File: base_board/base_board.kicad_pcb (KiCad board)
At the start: 6 copper layers, 50 x 50 mm, 54 parts, among them J1 Conn_ARM_JTAG_SWD_20, J2 Conn_01x20_Pin, J3 Conn_01x20_Socket, SW1 SW_Push, U1 STM32F446ZEJx, U2 IS42S16400J-xT, U3 BMI270, U4 USB_C_Receptacle_USB2.0, U5 10p, U6 10p, U7 LD3985M33R_SOT23, Y1 Crystal_GND24

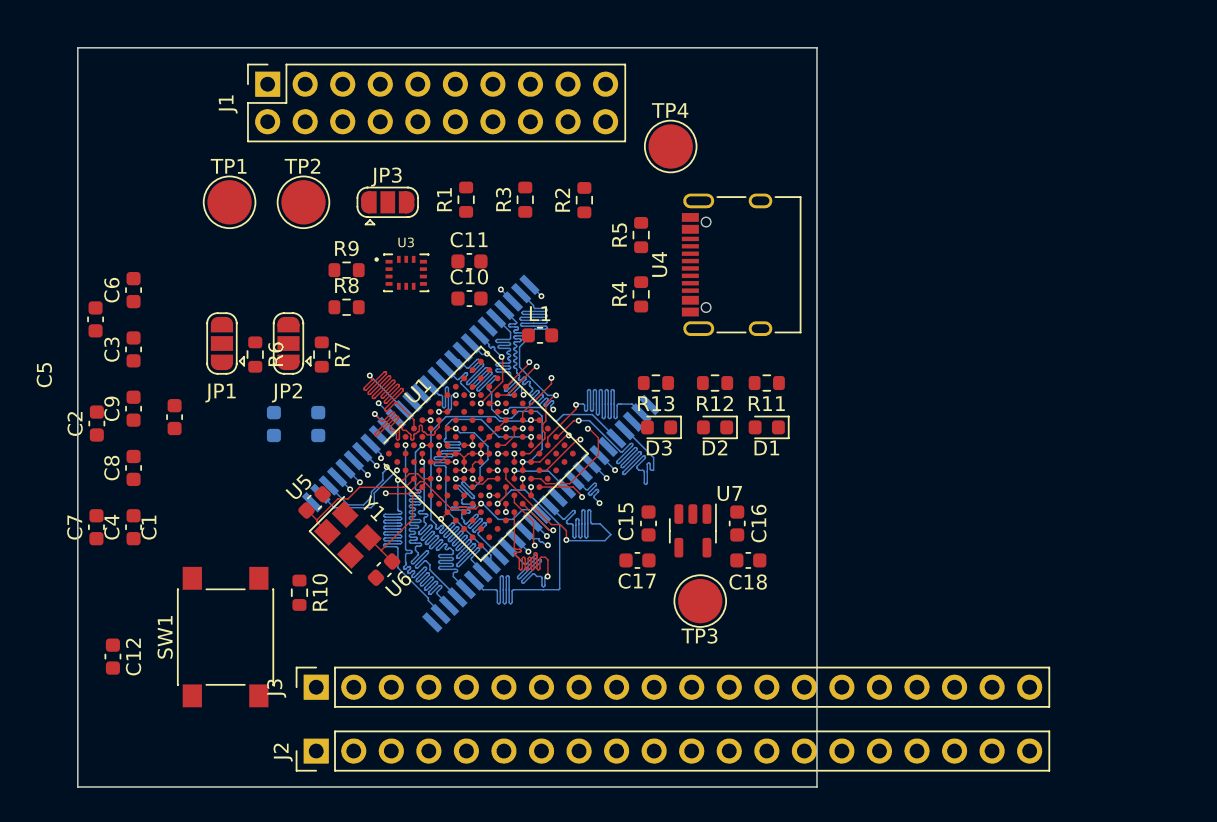
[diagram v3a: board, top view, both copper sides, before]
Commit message: [pcb] added route for BMI270
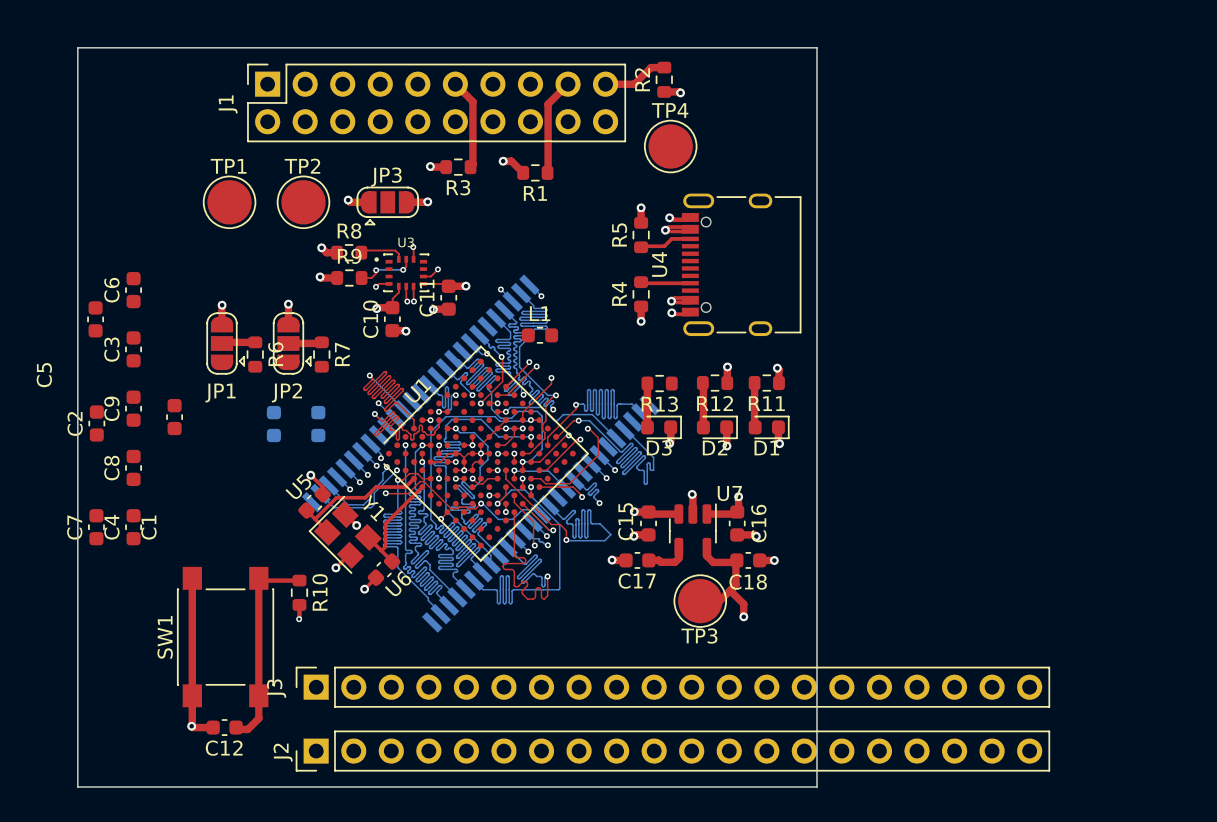
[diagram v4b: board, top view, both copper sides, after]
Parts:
- moved R2 9.78 mm to (142.7, 70.2)
- moved C12 8.95 mm to (112.9, 114.0), turned to 180 degrees
- moved C10 5.39 mm to (124.3, 86.4), turned to 90 degrees
- moved R3 5.03 mm to (128.7, 76.1), turned to 180 degrees
- moved R1 5.02 mm to (133.9, 76.5), turned to 180 degrees
- moved R8 3.69 mm to (121.4, 81.9)
- moved C11 2.83 mm to (128.1, 84.9), turned to 90 degrees
- moved R9 0.56 mm to (121.4, 83.6)
- moved R13 0.25 mm to (142.4, 90.7)
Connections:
- C10 pad 2: +3.3V -> +3V3
- C11 pad 2: +3.3V -> +3V3
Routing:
- net +3V3: track 0.00 -> 124.2 mm, vias 0 -> 11
- net +5V: track 0.00 -> 48.3 mm, vias 0 -> 5
- net GND: track 7.01 -> 47.1 mm, vias 6 -> 31
- net /RESET: track 0.00 -> 14.2 mm
- net Net-(J1-DBGRQ/NC): track 0.00 -> 6.57 mm
- net Net-(J1-RTCK): track 0.00 -> 6.17 mm
- net Net-(J1-DBGACK/NC): track 0.00 -> 4.44 mm
- net /BMI270_SCL: track 0.00 -> 3.96 mm, vias 0 -> 2
- net Net-(U4-CC2): track 0.00 -> 3.56 mm
- net Net-(U4-CC1): track 0.00 -> 3.36 mm
- net /BMI270_SDA: track 0.00 -> 3.06 mm
- net Net-(D2-A): track 0.00 -> 3.02 mm
- net Net-(D1-A): track 0.00 -> 3.02 mm
- net Net-(D3-A): track 0.00 -> 2.97 mm
- net Net-(U7-BYP): track 0.00 -> 2.94 mm
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
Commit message: Implemented SDRAM routing (#1)
* [pcb] completed sdram routing

* [pcb] added heartbeat led traces

* [pcb] completed routing except VDDUSB

* [pcb] changed routing for 5V power bus

* [pcb] fixed drc violation

* [pcb] added caps for VDDUSB

* [pcb] draft length matching

* [pcb] fixed length matching for sdram memory

* [view][pcb] toggled all layers for pcb

* [pcb] fixed power planes. Fixed traces shape

* [pcb] added review corrections

* [pcb] added M3 holes

* [pcb] added M3 holes

* [pcb] added onboard uart

* [pcb] added gnd+3v3 for uart socket

* [pcb][schematic] fixed VREF connection. Corrected the shape of the length matcher

* [project] updated fp-info-cache

* [pcb] fixed length matching pattern

* [pcb] placed sdram chip at 45 degree angle

* [project] updated fp-info cache
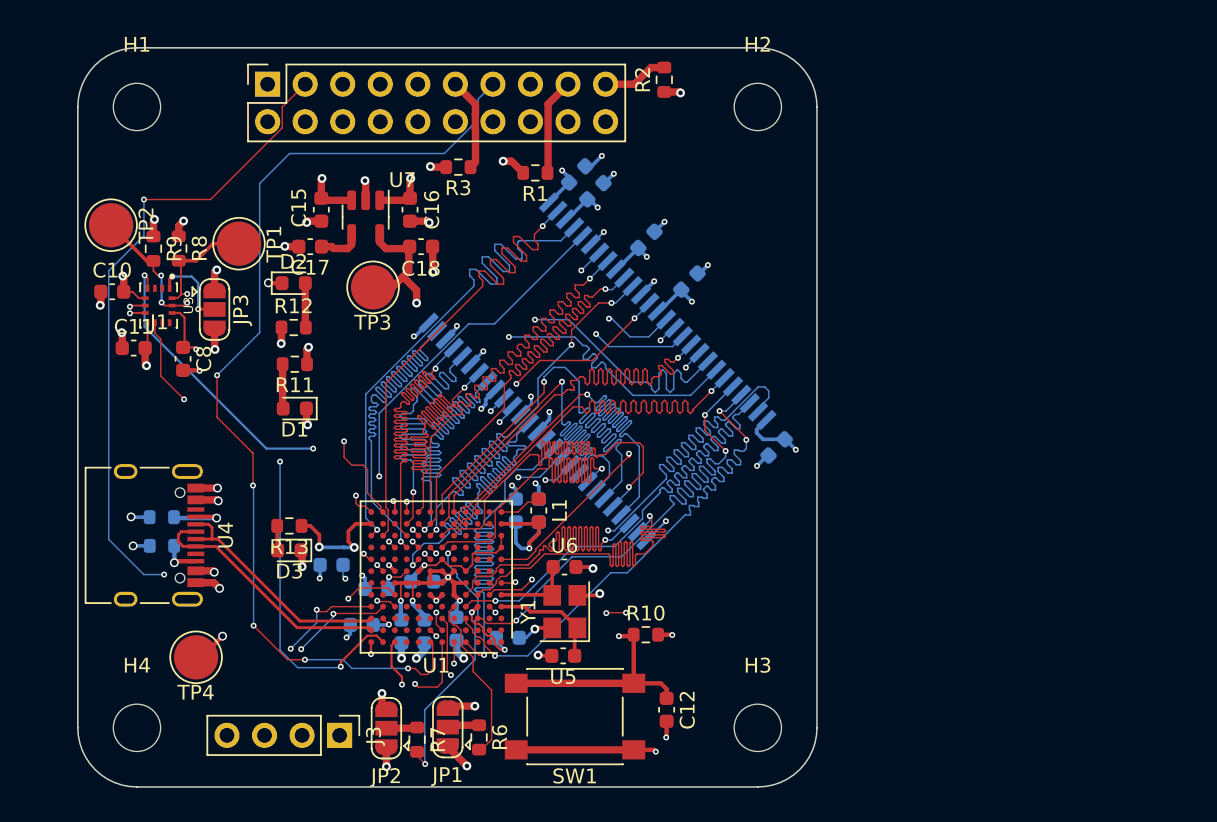
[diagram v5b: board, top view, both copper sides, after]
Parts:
- removed J2: Conn_01x20_Pin, Connector_PinHeader_2.54mm:PinHeader_1x20_P2.54mm_Vertical
- added C19: 100nF, Capacitor_SMD:C_0603_1608Metric, B.Cu at (144.4, 83.8)
- added C20: 100nF, Capacitor_SMD:C_0603_1608Metric, B.Cu at (132.1, 107.9)
- added C21: 1uF, Capacitor_SMD:C_0603_1608Metric, B.Cu at (132.6, 99.3)
- added C22: 100nF, Capacitor_SMD:C_0603_1608Metric, B.Cu at (122.2, 107.0)
- added C23: 100nF, Capacitor_SMD:C_0603_1608Metric, B.Cu at (134.2, 99.3)
- added H1: MountingHole, MountingHole:MountingHole_3.2mm_M3, F.Cu at (107.0, 72.0)
- added H2: MountingHole, MountingHole:MountingHole_3.2mm_M3, F.Cu at (149.0, 72.0)
- added H3: MountingHole, MountingHole:MountingHole_3.2mm_M3, F.Cu at (149.0, 114.0)
- added H4: MountingHole, MountingHole:MountingHole_3.2mm_M3, F.Cu at (107.0, 114.0)
- C1, C2, C3, C4, C5, C6, C7, C9, R4, R5: moved to B.Cu
- J3: value Conn_01x20_Socket -> Conn_01x04; footprint Connector_PinSocket_2.54mm:PinSocket_1x20_P2.54mm_Vertical -> Connector_PinHeader_2.54mm:PinHeader_1x04_P2.54mm_Vertical
- moved TP4 47.2 mm to (111.0, 109.2), turned to 180 degrees
- moved C7 46.3 mm to (150.3, 95.0), turned to -135 degrees
- moved U4 44.7 mm to (107.3, 101.0), turned to -90 degrees
- moved R5 38.6 mm to (108.7, 101.7), turned to 180 degrees
- moved C9 36.5 mm to (141.5, 81.0), turned to 45 degrees
- moved R4 35.8 mm to (108.7, 99.8), turned to 0 degrees
- moved C5 34.0 mm to (136.8, 76.6), turned to 45 degrees
- moved D1 32.0 mm to (117.7, 92.4)
- moved R11 32.0 mm to (117.7, 89.4)
- moved C6 31.9 mm to (138.0, 77.7), turned to 45 degrees
- moved C15 30.7 mm to (119.5, 79.0)
- moved C16 30.7 mm to (125.5, 79.0)
- moved C17 30.7 mm to (118.7, 81.5)
- moved C18 30.7 mm to (126.2, 81.5)
- moved TP3 30.7 mm to (123.0, 84.2)
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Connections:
- C1 pad 1: +3.3V -> +3V3
- C2 pad 1: +3.3V -> +3V3
- C3 pad 1: +3.3V -> +3V3
- C4 pad 1: +3.3V -> +3V3
- C5 pad 1: +3.3V -> +3V3
- C6 pad 1: +3.3V -> +3V3
- C7 pad 1: +3.3V -> +3V3
- C8 pad 1: +3.3V -> +3V3
- C9 pad 1: +3.3V -> +3V3
- J1 pad 1: +3.3V -> +3V3
- J1 pad 2: +3.3V -> +3V3
- J3 pad 1: /PC1 -> GND
- J3 pad 2: /PC2 -> /USART1_RX
- J3 pad 3: /PC3 -> /USART1_TX
- J3 pad 4: /PC4 -> +3V3
- L1 pad 2: +3.3V -> +3V3
- U1 pad C11: Net-(U1-VDDA) -> +3V3
- U1 pad D3: +3.3V -> +3V3
- U1 pad E5: +3.3V -> +3V3
- U1 pad F10: +3.3V -> +3V3
- U1 pad F4: +3.3V -> +3V3
- U1 pad F5: +3.3V -> +3V3
- U1 pad F6: +3.3V -> +3V3
- U1 pad F7: +3.3V -> +3V3
- U1 pad F8: +3.3V -> +3V3
- U1 pad F9: +3.3V -> +3V3
- U1 pad G5: +3.3V -> +3V3
- U1 pad G6: +3.3V -> +3V3
- U1 pad G7: +3.3V -> +3V3
- U1 pad K1: unconnected-(U1-VREF--PadK1) -> GND
- U1 pad L1: unconnected-(U1-VREF+-PadL1) -> +3V3
- U2 pad 1: Net-(U2-VDD-Pad1) -> +3V3
- U2 pad 14: Net-(U2-VDD-Pad1) -> +3V3
- U2 pad 27: Net-(U2-VDD-Pad1) -> +3V3
- U2 pad 3: Net-(U2-VDDQ-Pad3) -> +3V3
- U2 pad 43: Net-(U2-VDDQ-Pad3) -> +3V3
- U2 pad 49: Net-(U2-VDDQ-Pad3) -> +3V3
- U2 pad 9: Net-(U2-VDDQ-Pad3) -> +3V3
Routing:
- net /TRST: track 0.00 -> 71.1 mm, vias 0 -> 3
- net /SWO: track 0.00 -> 67.1 mm, vias 0 -> 5
- net /TDI: track 0.00 -> 62.2 mm, vias 0 -> 1
- net /SWDIO: track 0.00 -> 57.3 mm, vias 0 -> 1
- net /SWCLK: track 0.00 -> 54.7 mm, vias 0 -> 2
- net /RESET: track 14.2 -> 63.7 mm, vias 0 -> 2
- net +3V3: track 124.2 -> 80.5 mm, vias 11 -> 26
- net /BMI270_SDA: track 3.06 -> 39.2 mm, vias 0 -> 2
- net GND: track 47.1 -> 82.2 mm, vias 31 -> 53
- net +5V: track 48.3 -> 13.3 mm, vias 5 -> 6
- net /FMC_D6: track 4.58 -> 38.4 mm, vias 1 -> 3
- net /BMI270_SCL: track 3.96 -> 34.8 mm, vias 2 -> 4
- net /FMC_D2: track 9.37 -> 38.5 mm, vias 1 -> 2
- net /FMC_A4: track 10.7 -> 38.5 mm, vias 2 -> 1
- net /BMI270_INT1: track 0.97 -> 27.9 mm, vias 1 -> 3
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- added copper zone on In1.Cu, net +3V3
- added copper zone on In3.Cu, net +5V
- added copper zone on In4.Cu, net GND
- removed copper zone on In1.Cu, net +3.3V
- removed copper zone on In3.Cu, net GND
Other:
- outline, holes or cut-outs redrawn

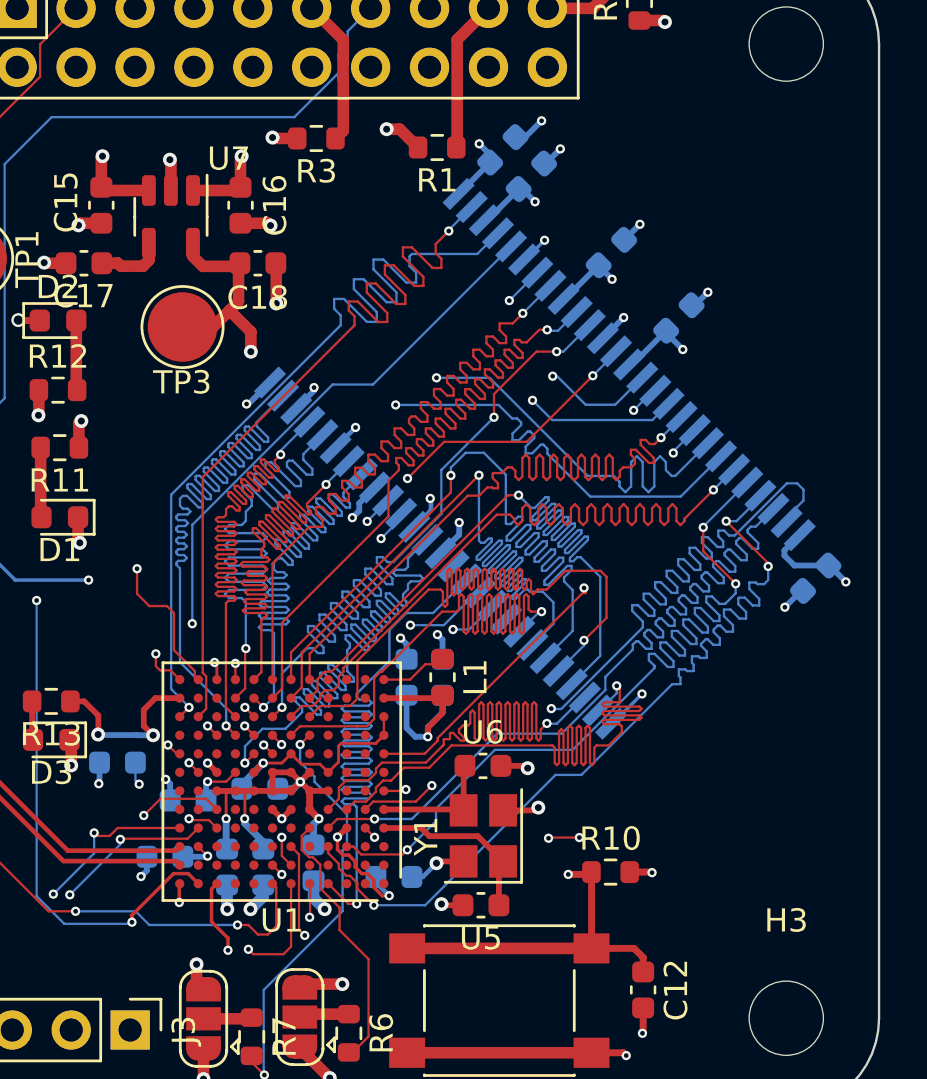
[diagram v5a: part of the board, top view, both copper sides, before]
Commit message: [pcb] cleanup of sdram routing
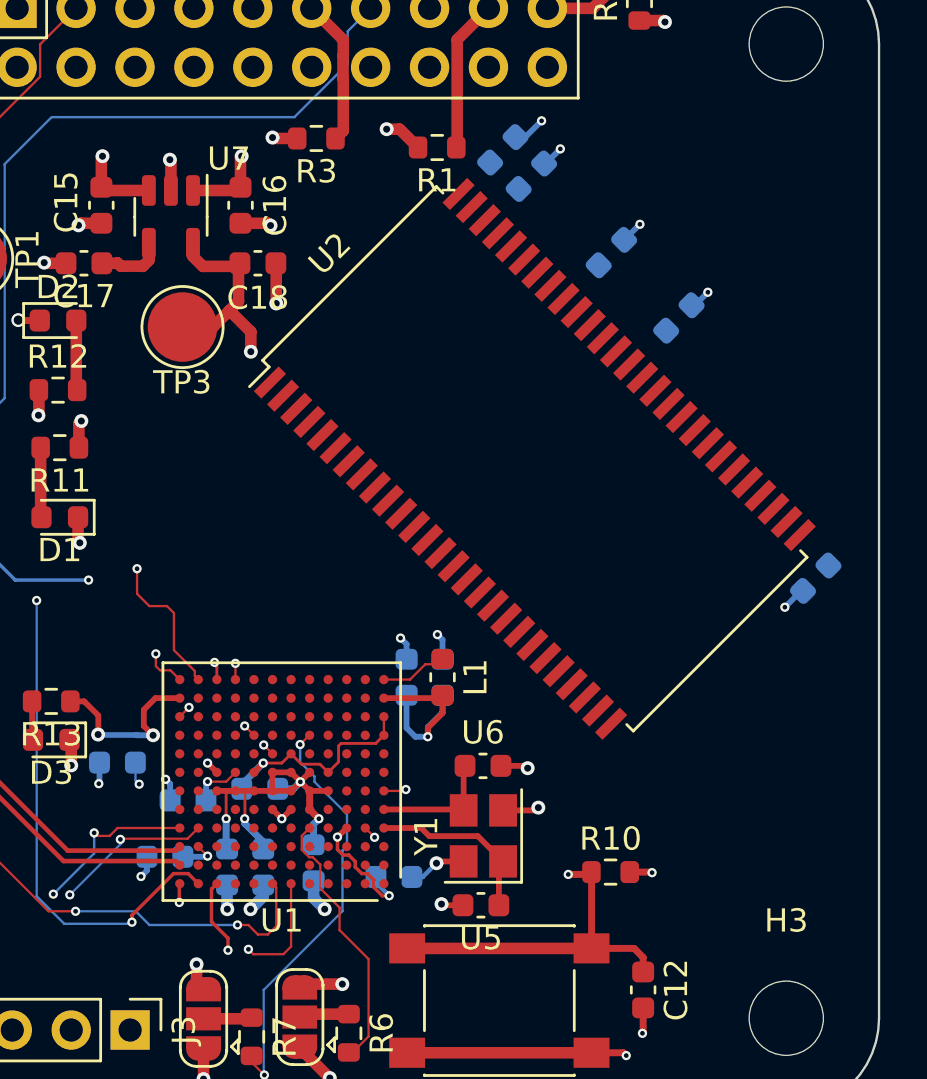
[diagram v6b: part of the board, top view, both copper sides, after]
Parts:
- U2: moved to F.Cu
- turned U2 to 45 degrees
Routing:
- net /FMC_D15: track 39.0 -> 0.00 mm, vias 1 -> 0
- net /FMC_SDKE1: track 38.9 -> 0.00 mm, vias 2 -> 0
- net /FMC_D10: track 38.8 -> 0.00 mm, vias 2 -> 0
- net /FMC_NBL1: track 38.8 -> 0.00 mm, vias 1 -> 0
- net /FMC_A11: track 38.8 -> 0.00 mm, vias 1 -> 0
- net /FMC_D11: track 38.7 -> 0.00 mm, vias 1 -> 0
- net /FMC_A6: track 38.7 -> 0.00 mm, vias 1 -> 0
- net /FMC_SDNWE: track 38.7 -> 0.00 mm, vias 2 -> 0
- net /FMC_SDCLK: track 38.6 -> 0.00 mm, vias 2 -> 0
- net /FMC_D2: track 38.5 -> 0.00 mm, vias 2 -> 0
- net /FMC_A9: track 38.5 -> 0.00 mm, vias 1 -> 0
- net /FMC_A4: track 38.5 -> 0.00 mm, vias 1 -> 0
- net /FMC_D0: track 38.5 -> 0.00 mm, vias 1 -> 0
- net /FMC_D4: track 38.5 -> 0.00 mm, vias 1 -> 0
- net /FMC_A3: track 38.5 -> 0.00 mm, vias 2 -> 0
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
